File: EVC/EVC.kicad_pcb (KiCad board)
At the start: 4 copper layers, 31 parts, among them CN1 HC-ZH1.5-6AW, CN2 HC-ZH1.5-6AW, CN3 HC-ZH1.5-6AW, CN4 HC-ZH1.5-6AW, J1 USB4105-GF-A, U1 CH592X, U2 TCR2EF33_LMCT, U3 C30732.768NCXE20, U4 DRV8835DSSR, U5 DRV8835DSSR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

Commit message: done
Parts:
- removed C4: 0.1uF, Footprint:C_0603
- removed C5: 1uF, Footprint:C_0603
- removed C7: 0.5pf, Footprint:C_0603
- removed C8: 1.5pf, Footprint:C_0603
- removed L2: 3.9nh, Footprint:0603
- removed U2: TCR2EF33_LMCT, Footprint:voltage regulator
- removed U3: C30732.768NCXE20, EasyEDA:HC-49S_L7.2-W3.2
- removed U6: ANT3216LL00R2400A, EasyEDA:ANT-SMD_L3.2-W1.6
- added C15: 0.1uF, Footprint:C_0603, F.Cu at (79.0, 73.4)
- added C16: 0.1uF, Footprint:C_0603, F.Cu at (75.9, 72.2)
- added C17: 10uf, Footprint:C_0603, F.Cu at (79.0, 72.2)
- added C18: 10uf, Footprint:C_0603, F.Cu at (75.9, 73.4)
- added J2: screen, Footprint:PinHeader_01x04_P2.54mm_Vertical_THT_D1mm, B.Cu at (73.9, 60.7)
- added P1: WJ500V-5.08-2P-14-00A, EasyEDA:CONN-TH_2P-P5.00_WJ500V-5.08-2P, F.Cu at (82.9, 56.3)
- added Q1: AMS1117-3.3V_C5120796, EasyEDA:SOT-89-3_L4.5-W2.5-P1.50-LS4.2-BR, F.Cu at (78.3, 76.3)
- added S1: TL3365AF180QG, Footprint:button, F.Cu at (84.3, 44.5)
- added S3: TL3365AF180QG, Footprint:button, F.Cu at (84.3, 48.6)
- added X1: Q13FC1350000400, EasyEDA:FC-135R_L3.2-W1.5, F.Cu at (66.3, 72.7)
- CN1: moved to B.Cu
- moved C10 50.3 mm to (65.0, 83.1), turned to -90 degrees
- moved L1 47.5 mm to (69.1, 76.2), turned to 180 degrees
- moved C9 45.9 mm to (69.5, 79.3)
- moved C12 43.1 mm to (71.2, 51.3), turned to 90 degrees
- moved C6 42.5 mm to (67.1, 77.5)
- moved C11 40.1 mm to (66.7, 83.0), turned to -90 degrees
- moved U4 39.1 mm to (68.2, 52.2), turned to 180 degrees
- moved C1 38.8 mm to (69.7, 77.5), turned to 180 degrees
- moved C14 37.7 mm to (70.2, 54.2)
- moved C13 35.2 mm to (72.8, 51.3), turned to 90 degrees
- moved C2 33.7 mm to (67.9, 66.0), turned to -90 degrees
- moved R1 33.7 mm to (81.3, 65.2), turned to 90 degrees
- moved R2 33.5 mm to (81.3, 70.6), turned to -90 degrees
- moved CN3 32.8 mm to (60.5, 37.1), turned to -120 degrees
- moved C3 32.5 mm to (68.0, 63.7)
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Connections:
- C10 pad 2: Net-(U5-VM) -> PWR_5V
- C11 pad 2: Net-(U5-VM) -> PWR_5V
- C12 pad 2: Net-(U4-VM) -> PWR_5V
- C13 pad 2: Net-(U4-VM) -> PWR_5V
- C14 pad 1: Net-(U4-MODE) -> VDD33
- C9 pad 1: Net-(U5-MODE) -> VDD33
- CN1 pad 1: unconnected-(CN1-Pad1) -> 3OUT2
- CN1 pad 2: unconnected-(CN1-Pad2) -> VDD33
- CN1 pad 3: unconnected-(CN1-Pad3) -> 3ENC1
- CN1 pad 4: unconnected-(CN1-Pad4) -> 3ENC2
- CN1 pad 5: unconnected-(CN1-Pad5) -> PWR_GND
- CN1 pad 6: unconnected-(CN1-Pad6) -> 3OUT1
- CN2 pad 1: unconnected-(CN2-Pad1) -> 2OUT1
- CN2 pad 2: unconnected-(CN2-Pad2) -> VDD33
- CN2 pad 3: unconnected-(CN2-Pad3) -> 2ENC1
- CN2 pad 4: unconnected-(CN2-Pad4) -> 2ENC2
- CN2 pad 5: unconnected-(CN2-Pad5) -> PWR_GND
- CN2 pad 6: unconnected-(CN2-Pad6) -> 2OUT2
- CN3 pad 1: unconnected-(CN3-Pad1) -> 4OUT1
- CN3 pad 2: unconnected-(CN3-Pad2) -> VDD33
- CN3 pad 3: unconnected-(CN3-Pad3) -> 4ENC1
- CN3 pad 4: unconnected-(CN3-Pad4) -> 4ENC2
- CN3 pad 5: unconnected-(CN3-Pad5) -> PWR_GND
- CN3 pad 6: unconnected-(CN3-Pad6) -> 4OUT2
- CN4 pad 1: 1OUT2 -> 1OUT1
- CN4 pad 6: 1OUT1 -> 1OUT2
- U1 pad 10: APH -> BPH
- U1 pad 17: unconnected-(U1-PB7/TXD0/PWM9-Pad17) -> SCL/CT10
- U1 pad 18: unconnected-(U1-PB4/RXD0/PWM7-Pad18) -> SDA/CT1
- U1 pad 24: ANT -> unconnected-(U1-ANT-Pad24)
- U1 pad 26: 3ENC1 -> 3ENC2
- U1 pad 27: 3ENC2 -> 3ENC1
- U1 pad 9: BPH -> APH
- U4 pad 1: Net-(U4-VM) -> PWR_5V
- U4 pad 11: Net-(U4-MODE) -> VDD33
- U4 pad 12: Net-(U4-MODE) -> VDD33
- U5 pad 1: Net-(U5-VM) -> PWR_5V
- U5 pad 11: Net-(U5-MODE) -> VDD33
- U5 pad 12: Net-(U5-MODE) -> VDD33
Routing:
- net PWR_5V: track 0.00 -> 72.3 mm, vias 0 -> 12
- net SDA/CT1: track 0.00 -> 50.7 mm
- net 3ENC1: track 0.00 -> 49.0 mm, vias 0 -> 2
- net 3ENC2: track 0.00 -> 47.3 mm, vias 0 -> 2
- net 4ENC2: track 0.00 -> 46.4 mm, vias 0 -> 2
- net 4ENC1: track 0.00 -> 46.1 mm, vias 0 -> 2
- net SCL/CT10: track 0.00 -> 42.3 mm
- net PWR_GND: track 0.00 -> 35.4 mm, vias 33 -> 19
- net 3OUT2: track 0.00 -> 26.8 mm
- net BEN-1: track 0.00 -> 24.4 mm
- net AEN-1: track 0.00 -> 23.9 mm, vias 0 -> 2
- net BPH-1: track 0.00 -> 23.6 mm
- net 3OUT1: track 0.00 -> 23.4 mm
- net APH-1: track 0.00 -> 23.3 mm
- net 1ENC2: track 0.00 -> 23.2 mm, vias 0 -> 1
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- added copper zone on In1.Cu, net PWR_GND
- added copper zone on In2.Cu, net PWR_GND
- added copper zone on In2.Cu, net VDD33
- removed copper zone on B.Cu, net PWR_GND
- removed copper zone on F.Cu, net PWR_GND
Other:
- board outline added: 35.9 x 61.1 mm

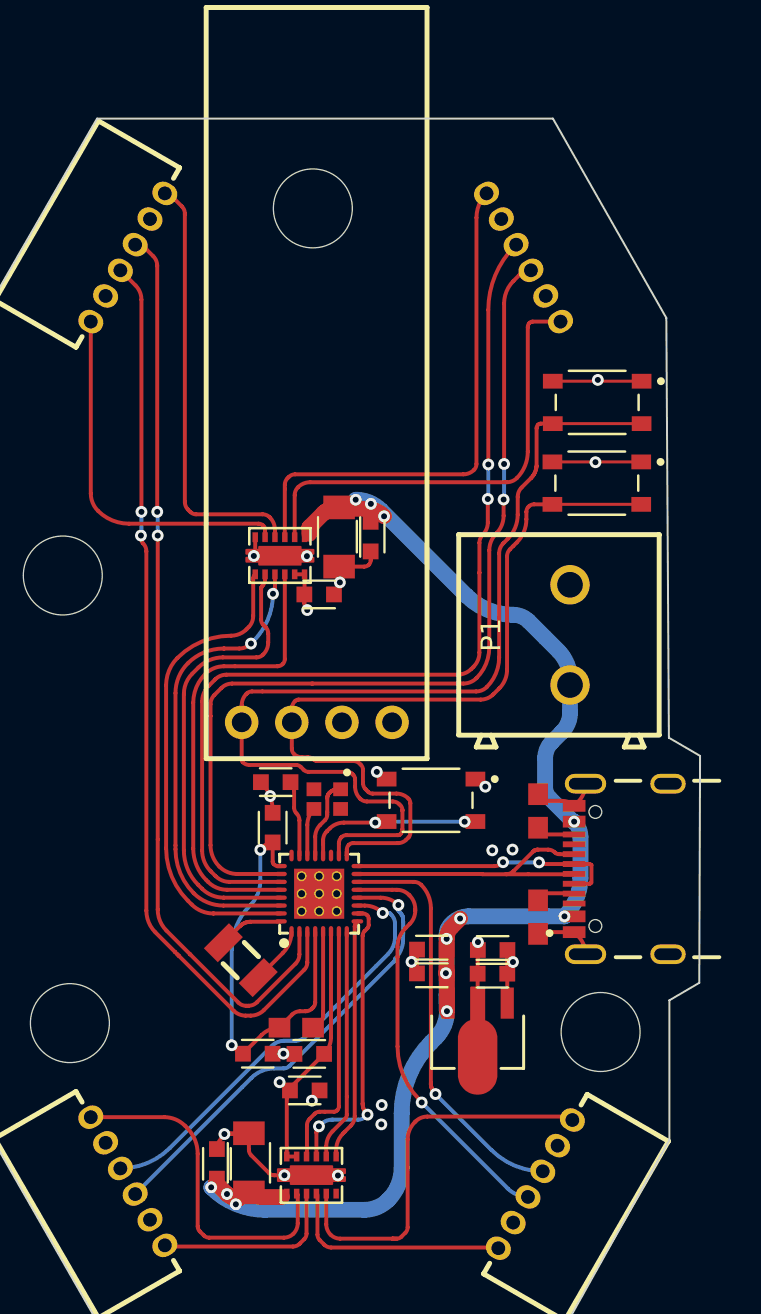
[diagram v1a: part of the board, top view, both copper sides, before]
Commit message: fixed that one connector + flipped screw terminal
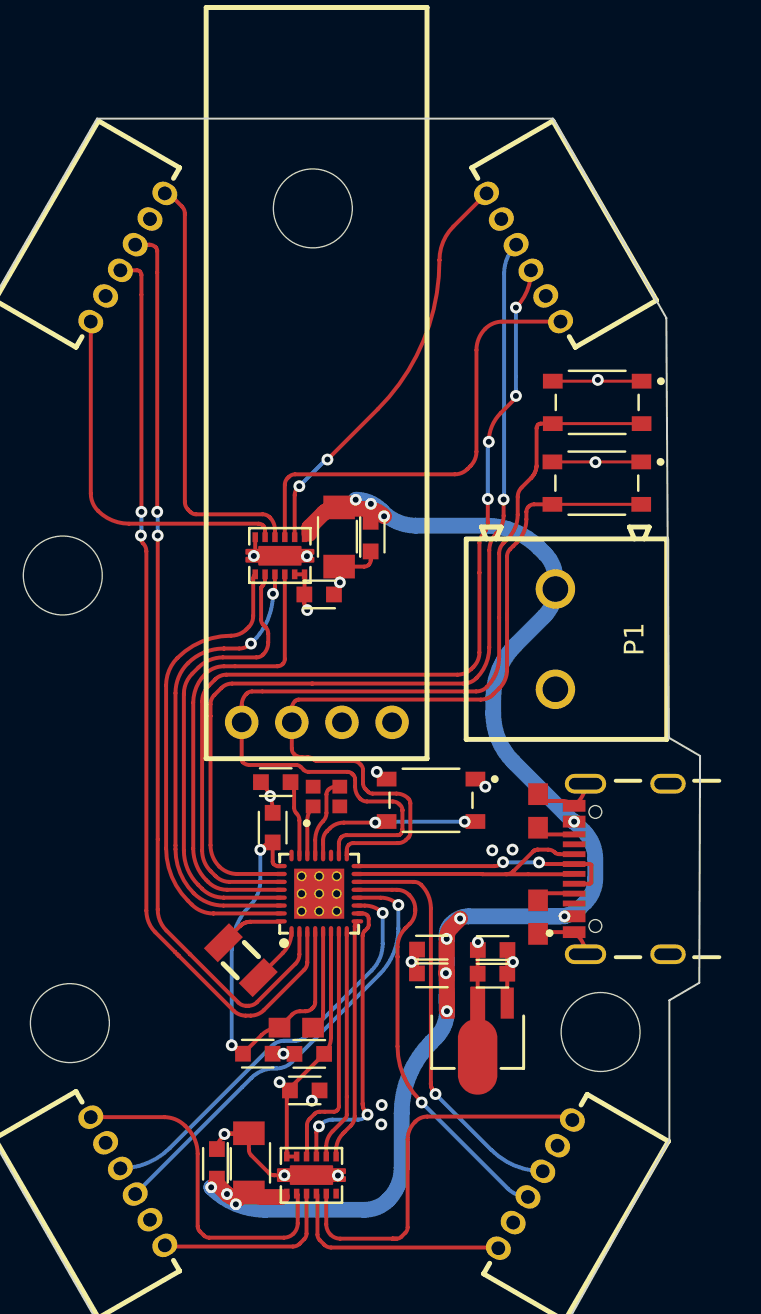
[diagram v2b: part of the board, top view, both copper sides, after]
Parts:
- CN1: moved to F.Cu
- moved P1 0.77 mm to (82.2, 56.5), turned to -90 degrees
- moved Y1 0.14 mm to (70.6, 64.5), turned to 90 degrees
- turned CN1 to 120 degrees
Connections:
- U1 pad 21: XI -> XO
- U1 pad 22: XO -> XI
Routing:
- net PWR_5V: track 72.3 -> 77.6 mm
- net 3OUT2: track 26.8 -> 23.5 mm
- net 3OUT1: track 23.4 -> 20.8 mm, vias 0 -> 2
- net XO: track 2.44 -> 4.12 mm
- net XI: track 4.01 -> 2.56 mm
- net 3ENC1: track 49.0 -> 48.0 mm, vias 2 -> 4
- net 3ENC2: track 47.3 -> 48.1 mm, vias 2 -> 1
- net 1ENC1: track 21.8 -> 21.1 mm
- net 4ENC2: track 46.4 -> 47.0 mm
